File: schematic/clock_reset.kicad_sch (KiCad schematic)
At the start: 13 parts, among them U22 74LS04, U7 74LS05

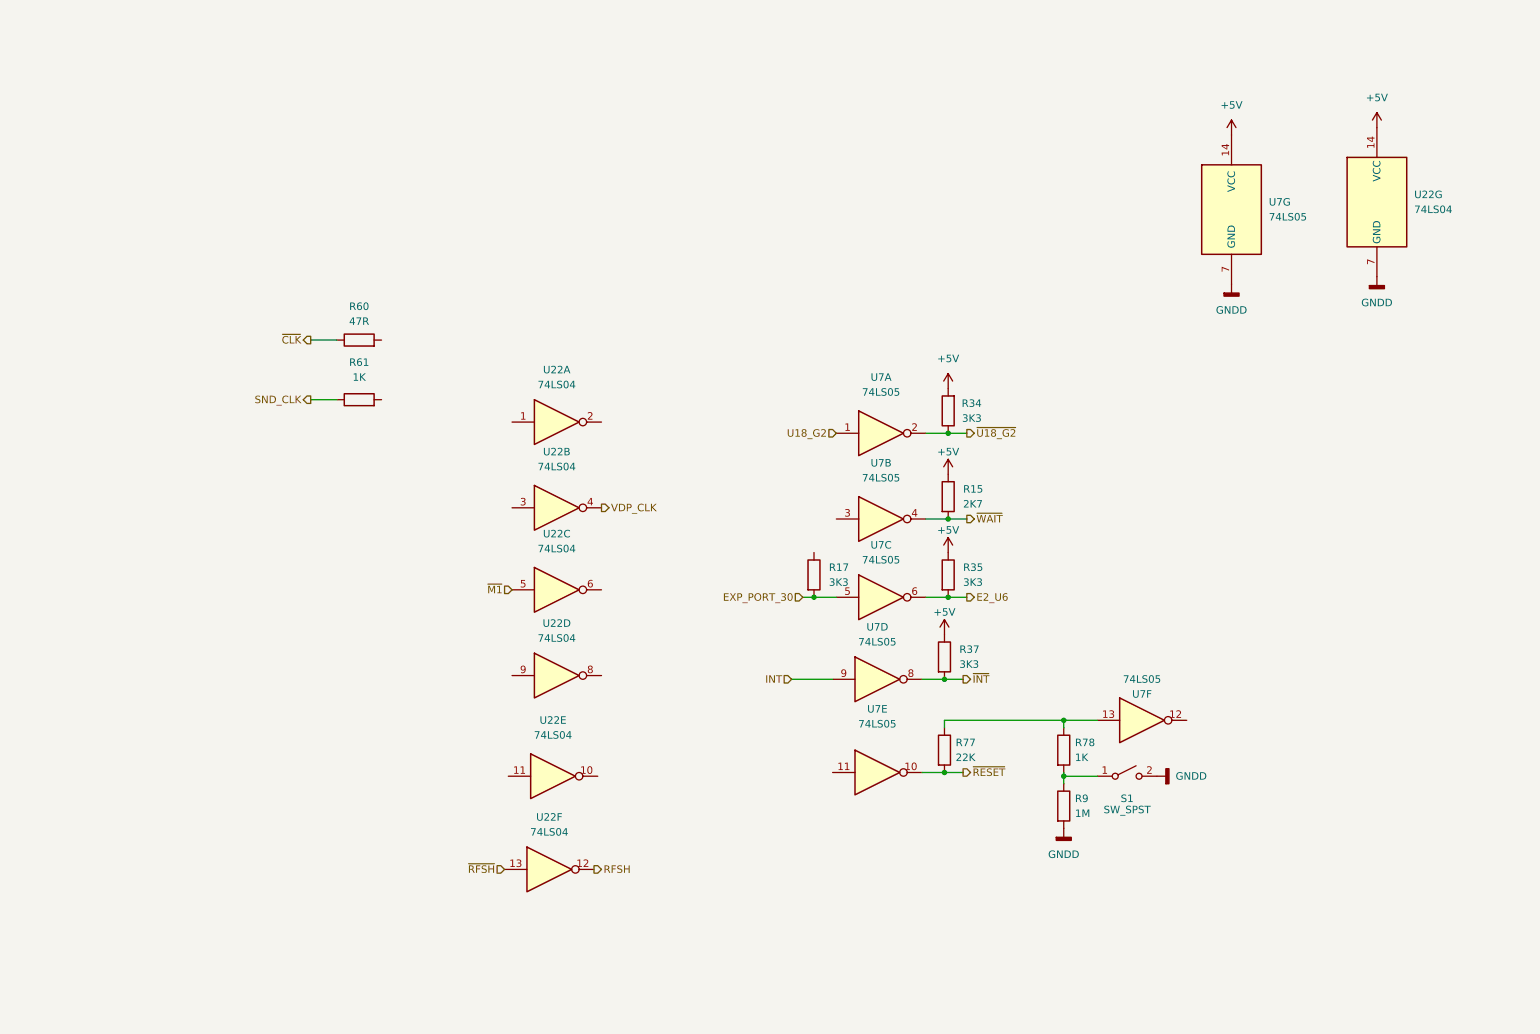
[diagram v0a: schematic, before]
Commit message: started work on clock_reset_misc circuits. inverter u7 done, u8 added and starting work around U22.
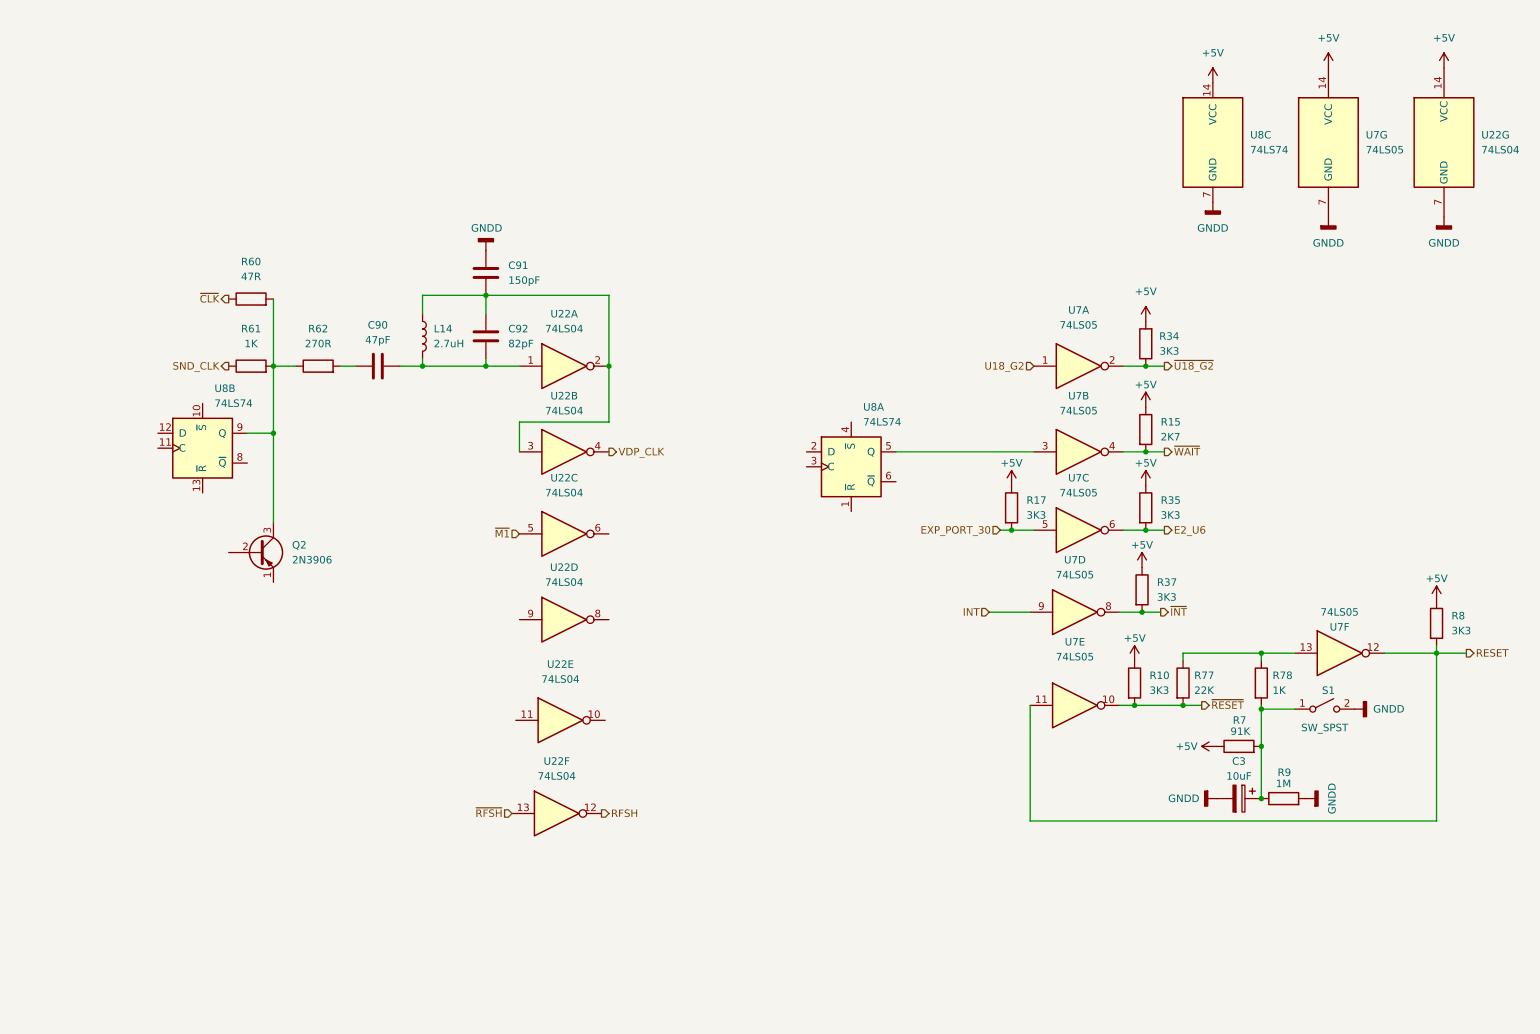
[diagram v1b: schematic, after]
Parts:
- added C3: 10uF, symbol Device:C_Polarized
- added C90: 47pF, symbol Device:C
- added C91: 150pF, symbol Device:C
- added C92: 82pF, symbol Device:C
- added L14: 2.7uH, symbol Device:L
- added Q2: 2N3906, Package_TO_SOT_THT:TO-92_Inline, symbol Transistor_BJT:2N3906
- added R10, R8: 3K3, symbol Device:R
- added R62: 270R, symbol Device:R
- added R7: 91K, symbol Device:R
- added U8: 74LS74, symbol 74xx:74LS74
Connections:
- net +5V: now also R17.1, R10.1, R7.1, R8.1, U8.14 (VCC)
- net GNDD: now also C3.2, C91.1, U8.7 (GND)
- net ~{RESET}: now also R10.2
- net at R78.2, R9.1, S1.1 (A): now also C3.1, R7.2
- net RESET: now reaches U7.11
- net RESET: now also U7.12, R8.2
- net at U7.3: now also U8.5 (Q)
- net at R60.2: now also R61.2, Q2.3 (C), R62.1, U8.9 (Q)
- net at U22.1: now also C90.2, C92.2, L14.2
- net at U22.2: now also U22.3, C91.2, C92.1, L14.1
- new net: C90.1, R62.2
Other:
- moved on the sheet: R15, R17, R34, R35, R37, R77, R78, R9, S1, U22A, U22B, U22C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

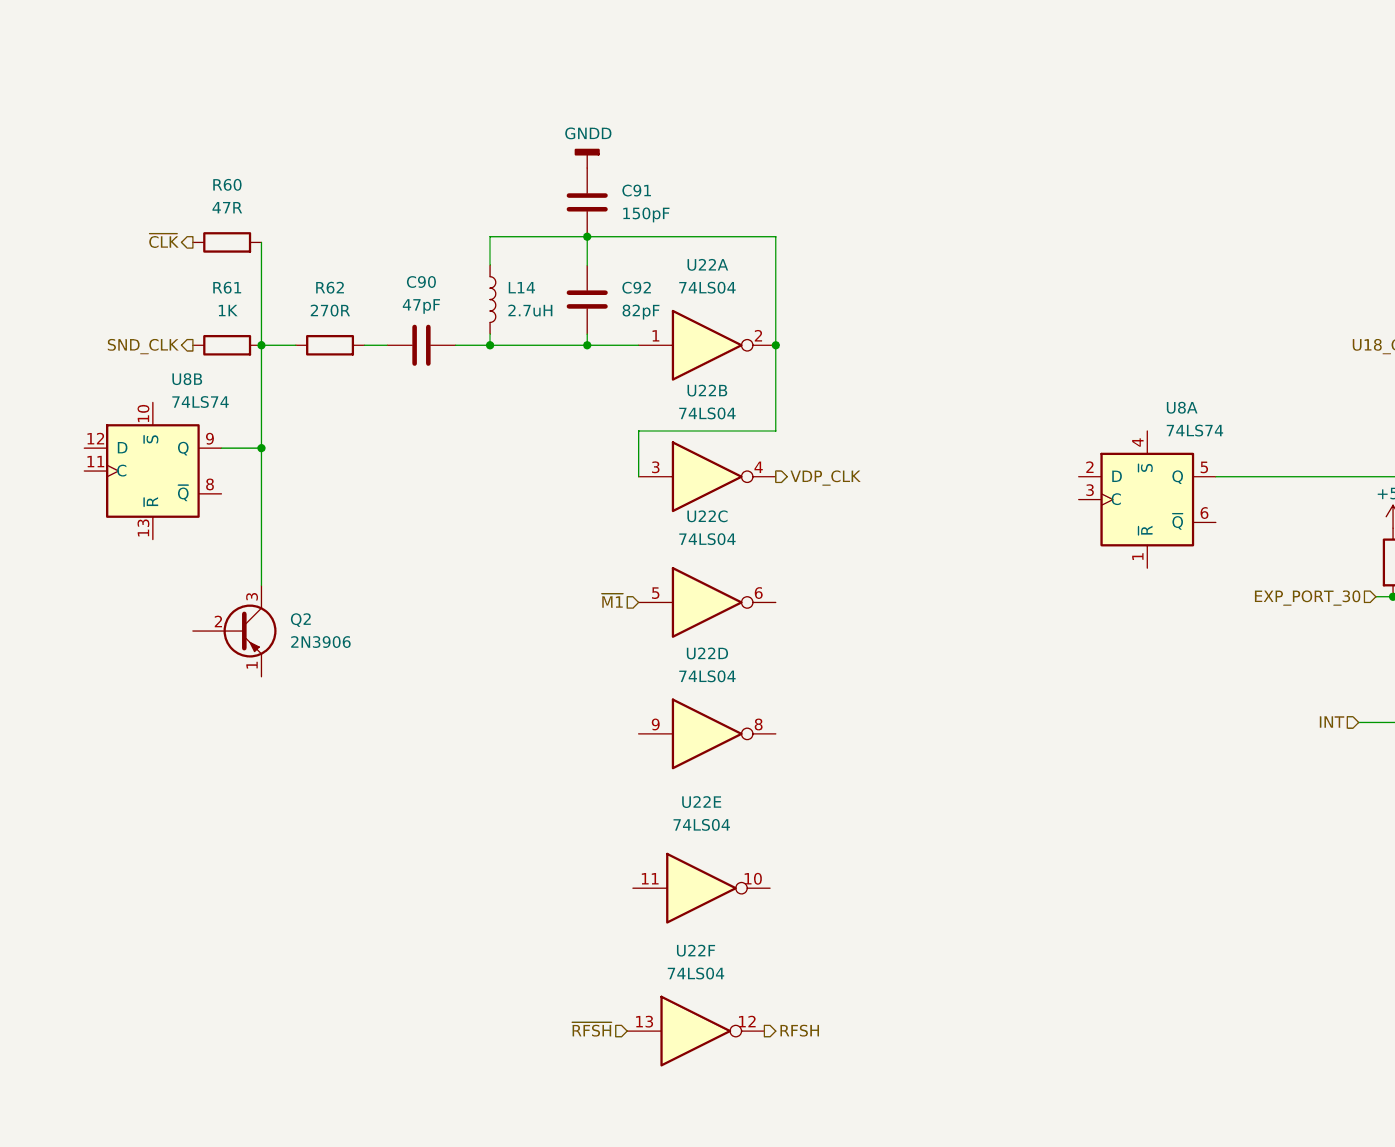
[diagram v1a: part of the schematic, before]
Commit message: first version of clock-reset circuits. Its a bit complicated and will need some revisions.
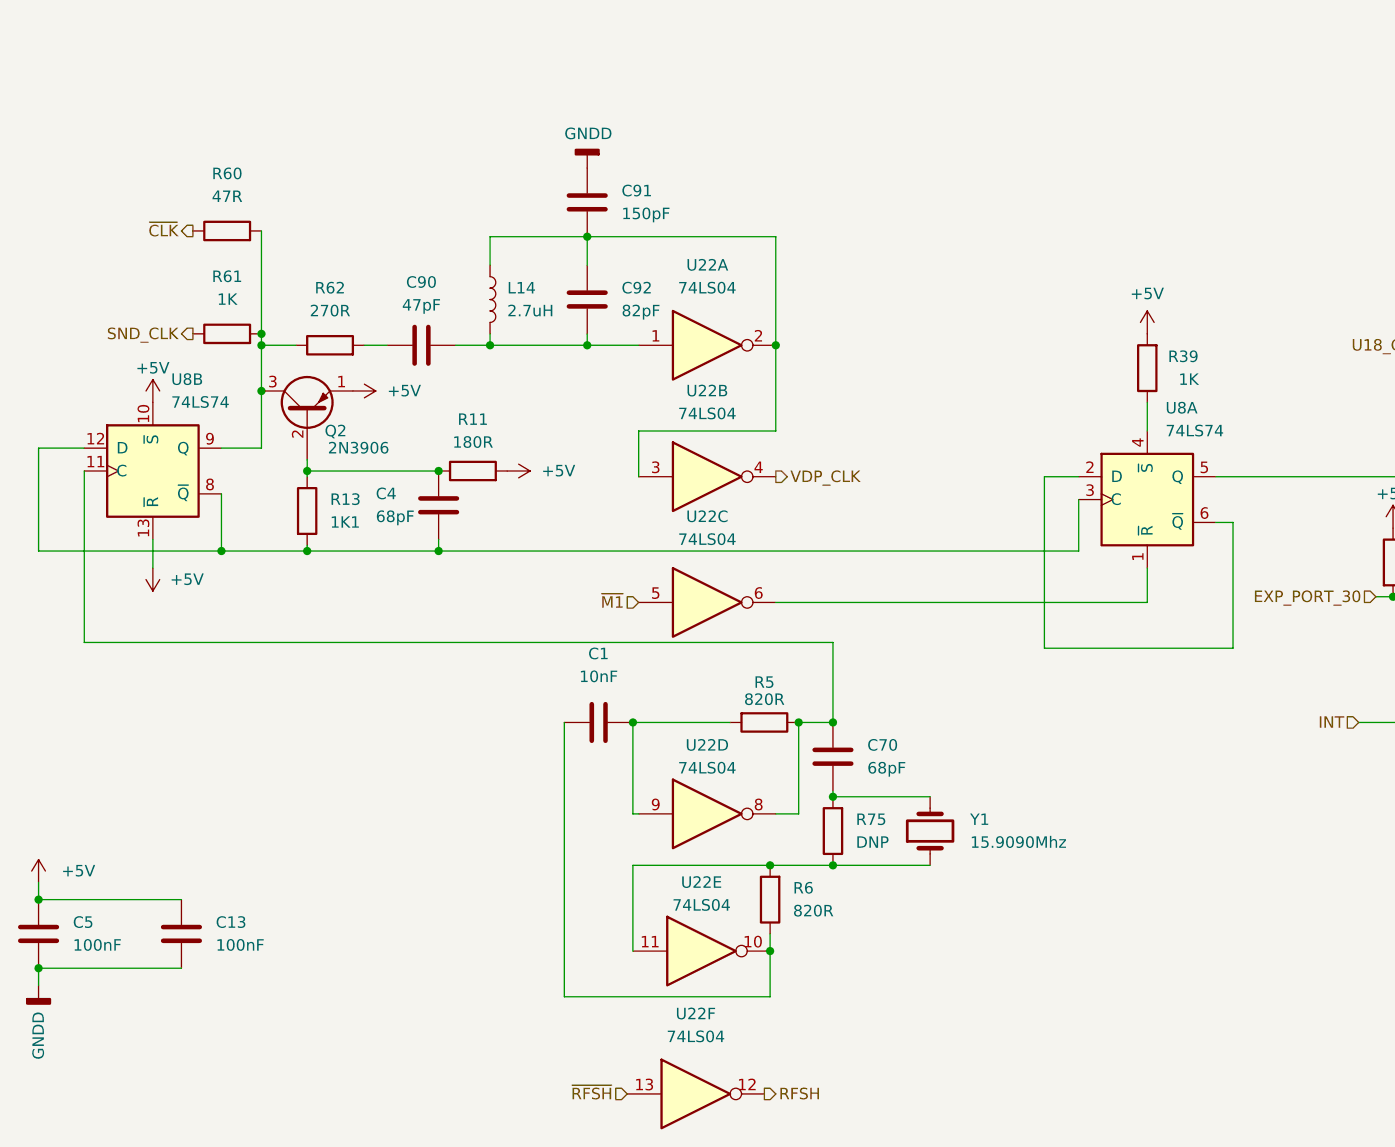
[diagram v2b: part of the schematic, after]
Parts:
- added C1: 10nF, symbol Device:C
- added C13, C5: 100nF, symbol Device:C
- added C4, C70: 68pF, symbol Device:C
- added R11: 180R, symbol Device:R
- added R13: 1K1, symbol Device:R
- added R39: 1K, symbol Device:R
- added R5, R6: 820R, symbol Device:R
- added R75: DNP, symbol Device:R
- added Y1: 15.9090Mhz, symbol Device:Crystal
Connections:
- net +5V: now also Q2.1 (E), U8.10 (~{S}), U8.13 (~{R}), C13.2, C5.2, R11.2, R39.2
- net GNDD: now also C13.1, C5.1
- net at U8.11 (C): now also U22.8, C70.1, R5.1
- net at U8.12 (D): now also U8.3 (C), U8.8 (~{Q}), C4.2, R13.2
- net at U8.1 (~{R}): now also U22.6
- net at U8.2 (D): now also U8.6 (~{Q})
- net at U8.4 (~{S}): now also R39.1
- net at U22.9: now also C1.2, R5.2
- net at Q2.2 (B): now also C4.1, R11.1, R13.1
- net at U22.10: now also C1.1, R6.1
- net at U22.11: now also R6.2, R75.1, Y1.1
- new net: C70.2, R75.2, Y1.2
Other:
- moved on the sheet: Q2, R60, R61, U22D, U22E, U22F

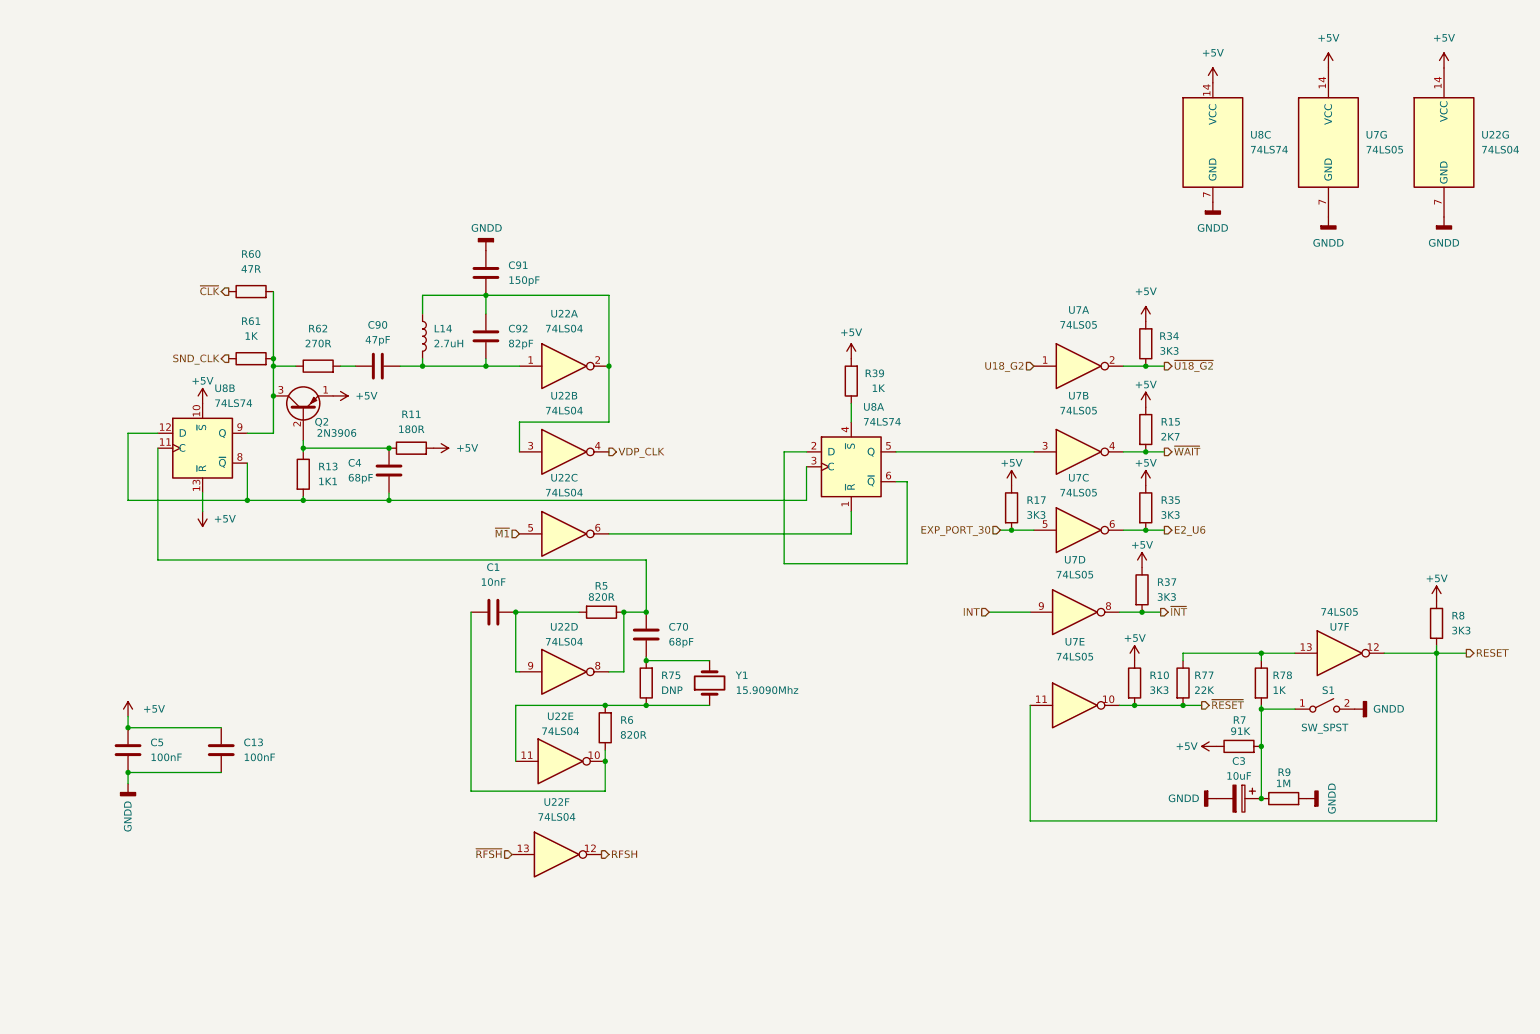
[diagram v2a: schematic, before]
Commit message: altered and did some cleanup of the way the wires were run. Finished expansion port routes to rf modulator. Added ext_psu for future external power supply design (will be an off the shelf psu block).
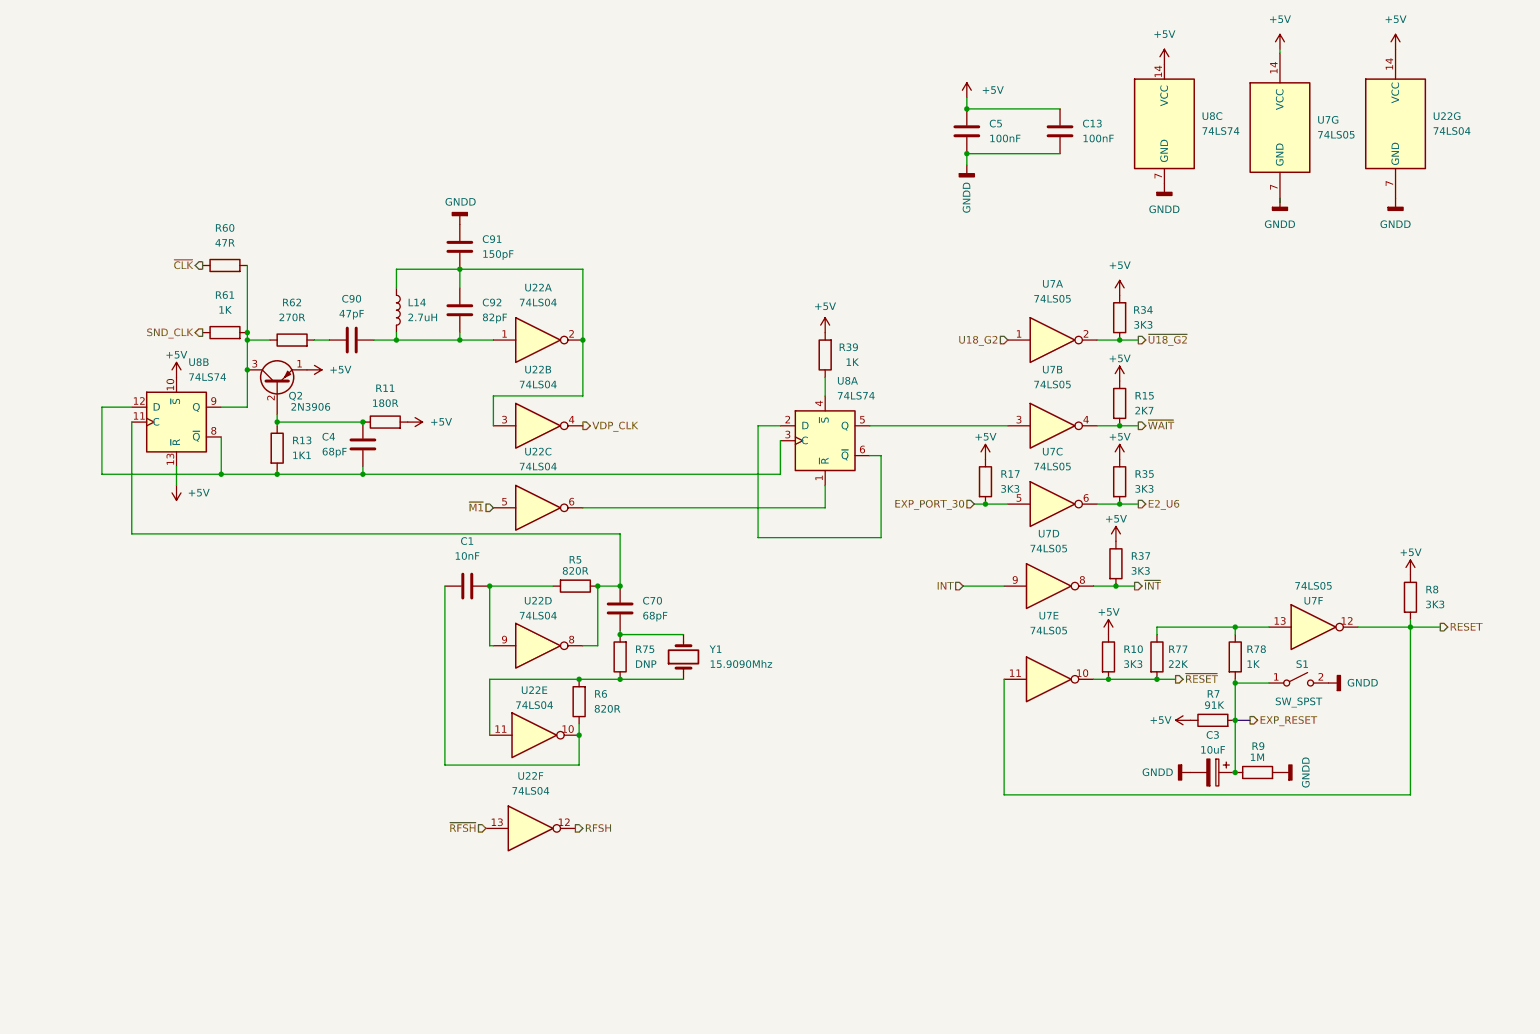
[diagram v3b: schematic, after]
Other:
- moved on the sheet: C1, C13, C3, C4, C5, C70, C90, C91, C92, L14, Q2, R10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
